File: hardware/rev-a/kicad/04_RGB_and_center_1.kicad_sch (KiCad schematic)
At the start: 16 parts, among them U7 NJM4580DD, U8 NJM4580DD

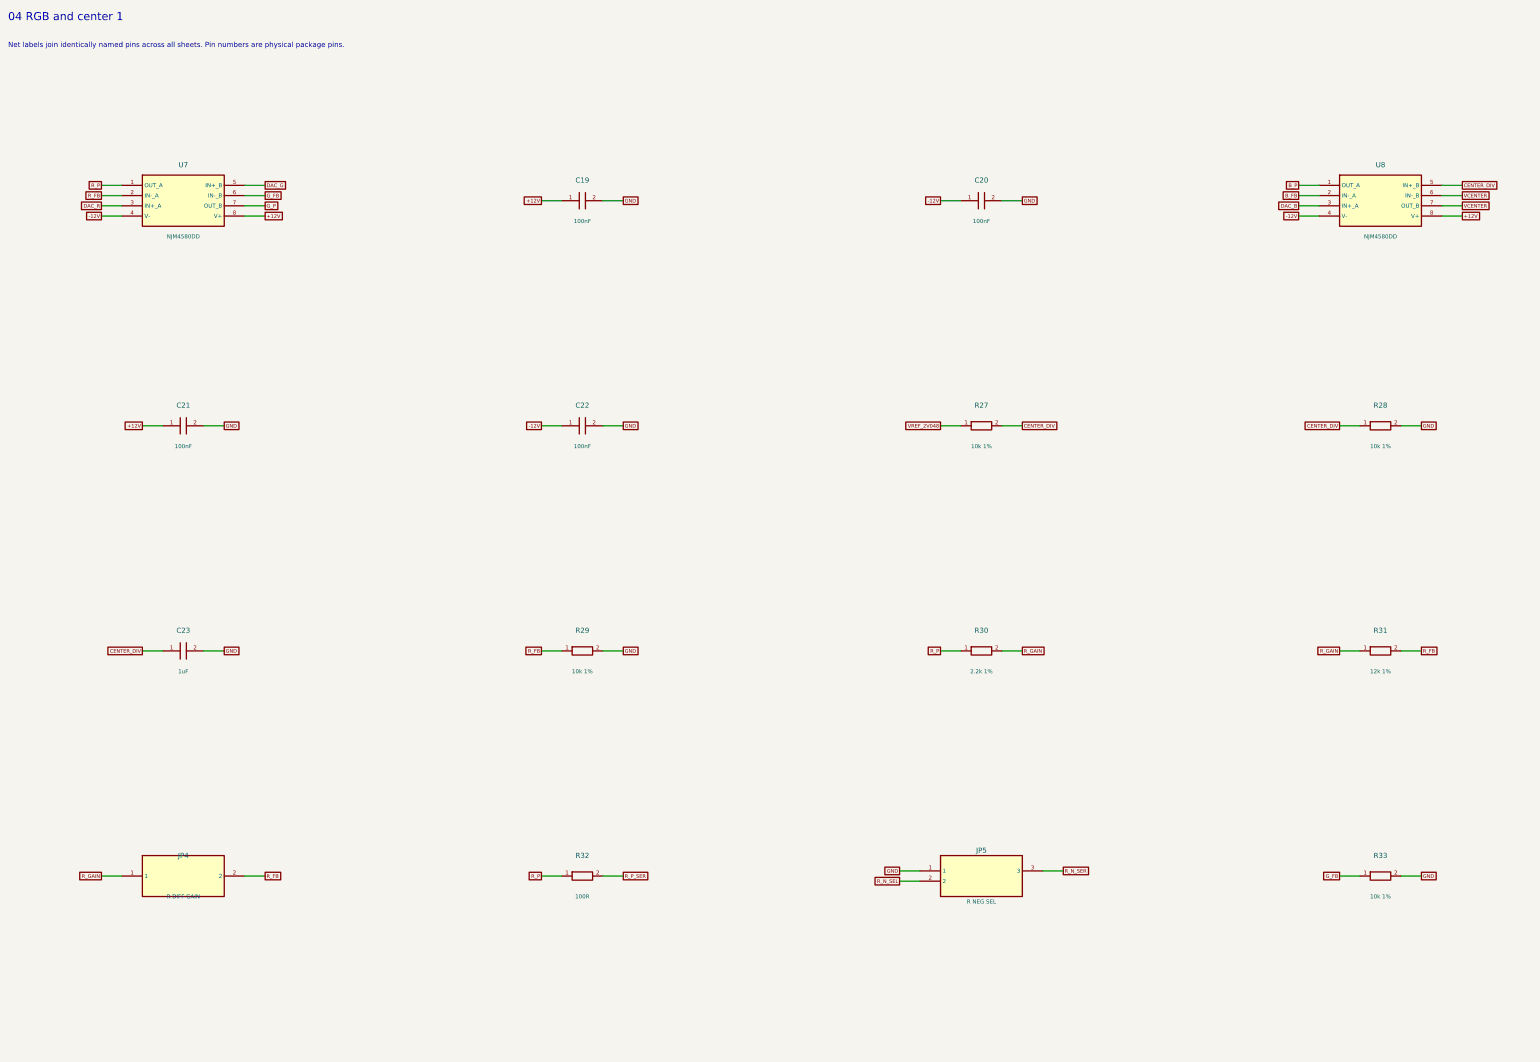
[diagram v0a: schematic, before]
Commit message: Redraw Rev.A schematics with functional blocks and explicit wiring
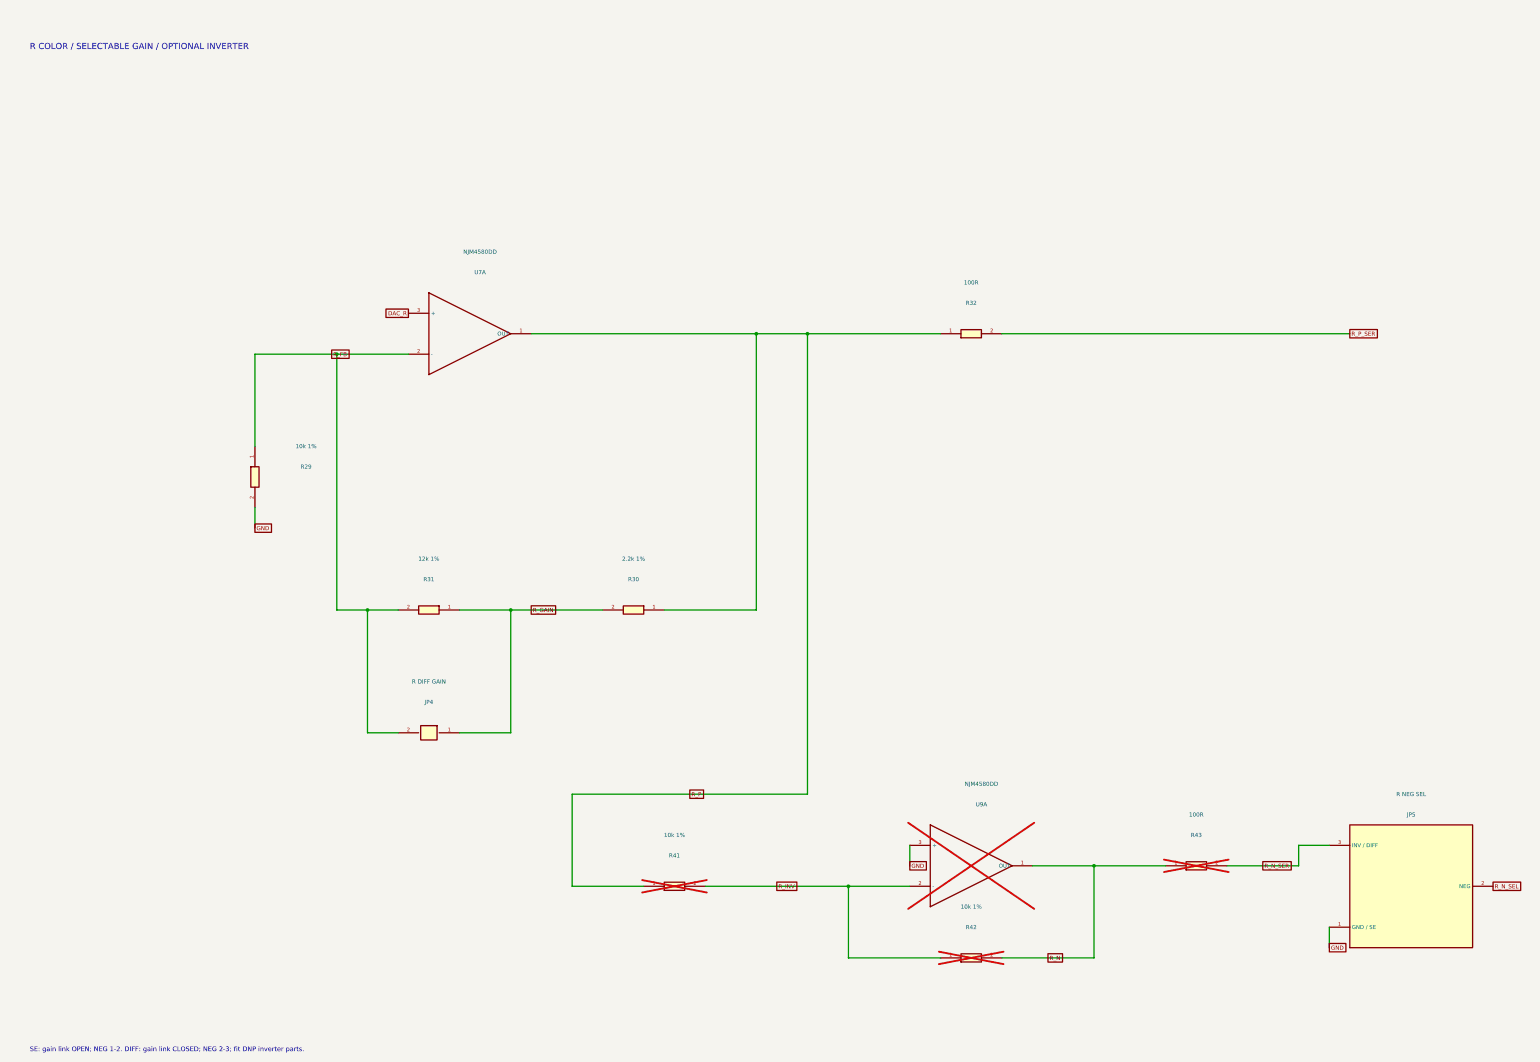
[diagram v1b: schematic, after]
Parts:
- removed C19, C20, C21, C22: 100nF, RevA:C_Disc_D5.0mm_W2.5mm_P5.00mm, symbol RevA:C
- removed C23: 1uF, RevA:C_Disc_D5.0mm_W2.5mm_P5.00mm, symbol RevA:C
- removed R27, R28, R33: 10k 1%, RevA:R_Axial_DIN0207_L6.3mm_D2.5mm_P10.16mm_Horizontal, symbol RevA:R
- removed U8: NJM4580DD, RevA:DIP-8_W7.62mm, symbol RevA:Opamp
- added R41, R42: 10k 1%, RevA:R_Axial_DIN0207_L6.3mm_D2.5mm_P10.16mm_Horizontal, symbol RevA:R
- added R43: 100R, RevA:R_Axial_DIN0207_L6.3mm_D2.5mm_P10.16mm_Horizontal, symbol RevA:R
- added U9: NJM4580DD, RevA:DIP-8_W7.62mm, symbol RevA:AMP
- JP4: symbol RevA:Conn_JP4 -> RevA:Link
- JP5: symbol RevA:Conn_JP5 -> RevA:Part_JP5
- U7: symbol RevA:Opamp -> RevA:AMP
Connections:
- net GND: now also U9.3 (+)
- net R_N_SER: now also R43.2
- net R_P: now also R41.1
- removed net +12V: U7.8 (V+)
- removed net -12V: U7.4 (V-)
- removed net DAC_G: U7.5 (IN+_B)
- removed net G_FB: U7.6 (IN-_B)
- removed net G_P: U7.7 (OUT_B)
- new net R_INV: R41.2, R42.1, U9.2 (-)
- new net R_N: R42.2, R43.1, U9.1 (OUT)
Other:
- note added: "R COLOR / SELECTABLE GAIN / OPTIONAL INVERTER"
- note added: "SE: gain link OPEN; NEG 1-2. DIFF: gain link CLOSED; NEG 2-3; fit DNP inverter parts."
- note removed: "04 RGB and center 1"
- note removed: "Net labels join identically named pins across all sheets. Pin numbers are physical package pins."
- company: CoreS3 ILDA evaluation -> (none)
- title: 04_RGB_and_center_1 -> R / Color driver and optional differential stage
- moved on the sheet: JP5
